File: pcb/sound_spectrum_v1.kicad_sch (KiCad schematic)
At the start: 33 parts, among them IC1-L1 ICS-43432, IC2-R1 ICS-43432, J1 SWD_CONN, J2 Conn_02x10_Counter_Clockwise, P1 USB_C_Plug_USB2.0, SW2 SW_DPST_x2, U1 STM32G473CBTx, U2 AP2112K-3.3, U3 USBLC6-2SC6, Y2 SG-210STF 48.0000ML5

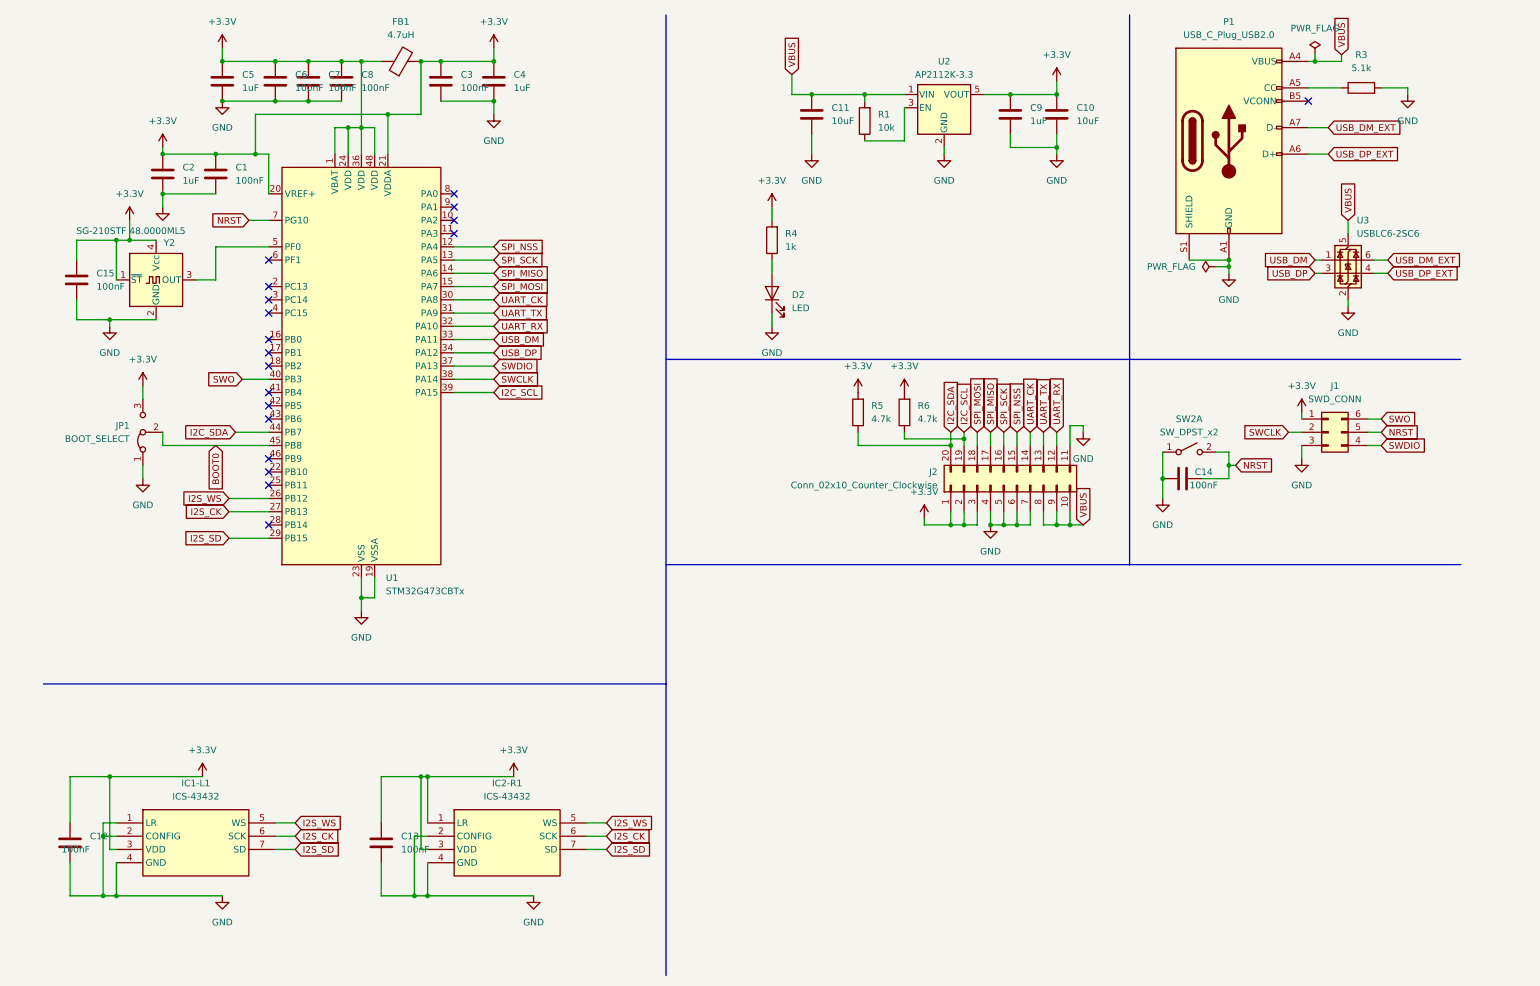
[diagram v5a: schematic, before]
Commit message: feat: add mounting holes
chore: change usb c receptor

chore: align microphones
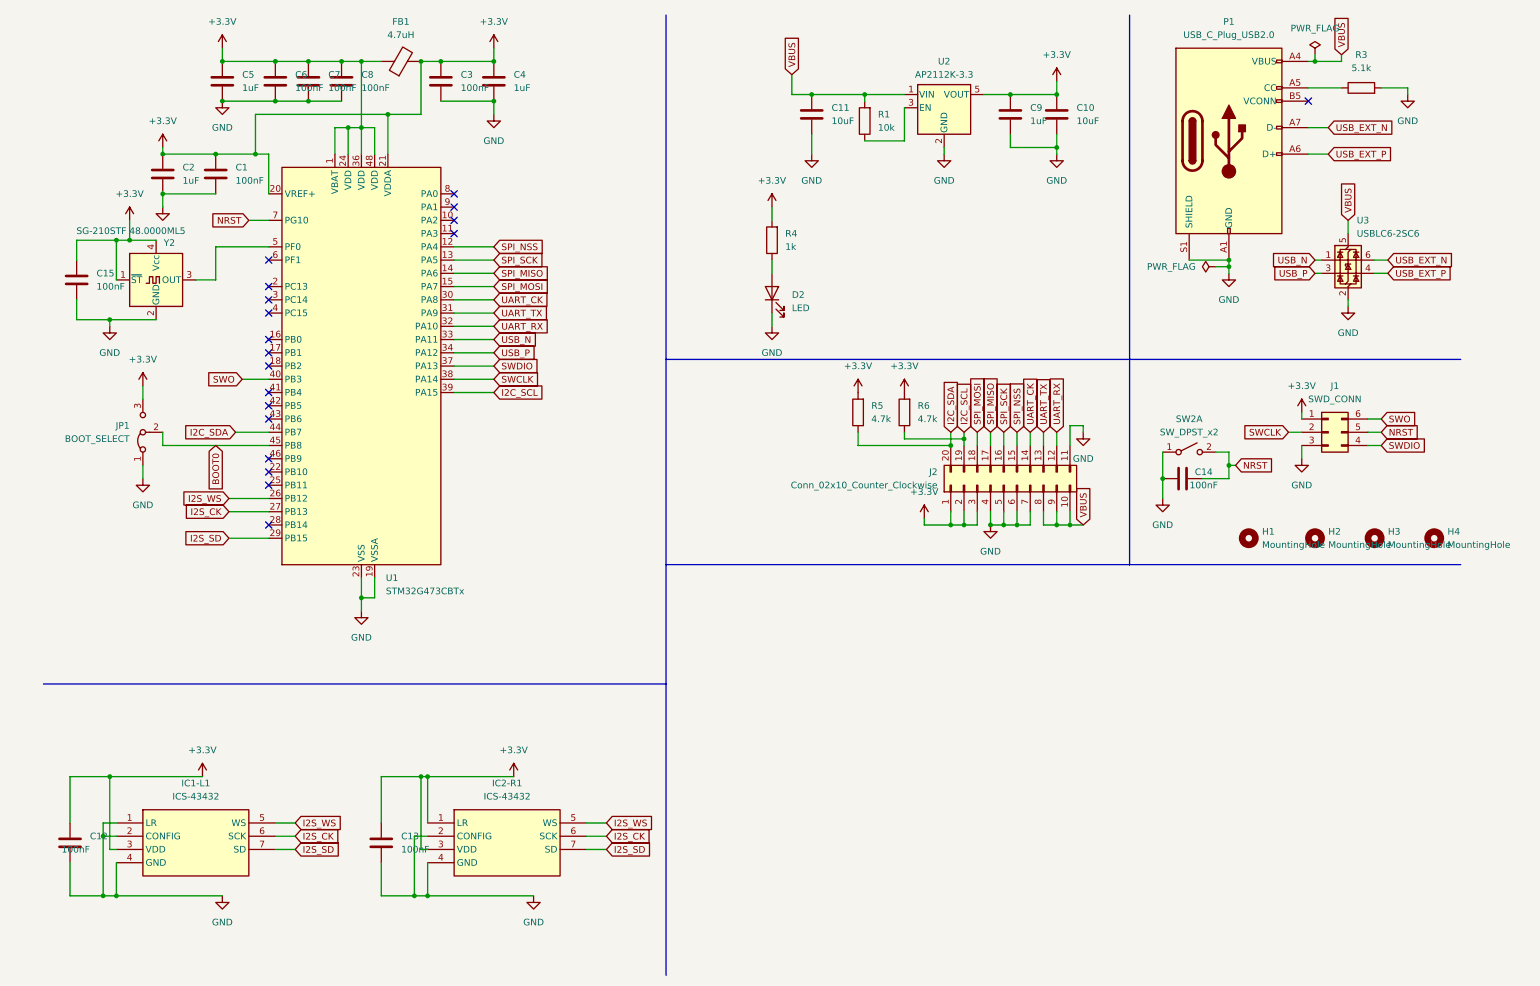
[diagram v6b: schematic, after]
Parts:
- added H1, H2, H3, H4: MountingHole, MountingHole:MountingHole_3.2mm_M3_DIN965, symbol Mechanical:MountingHole
- P1: footprint Connector_USB:USB_C_Receptacle_GCT_USB4085 -> Connector_USB:USB_C_Receptacle_GCT_USB4105-xx-A_16P_TopMnt_Horizontal
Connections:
- net USB_DM renamed USB_N
- net USB_DM_EXT renamed USB_EXT_N
- net USB_DP renamed USB_P
- net USB_DP_EXT renamed USB_EXT_P

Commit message: chore: add extra led
chore: minor changes
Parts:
- removed Y2: SG-210STF 48.0000ML5, Oscillator:Oscillator_SMD_SeikoEpson_SG210-4Pin_2.5x2.0mm, symbol Oscillator:SG-211
- added C16: 33pF, Capacitor_SMD:C_0805_2012Metric_Pad1.18x1.45mm_HandSolder, symbol Device:C
- added D1: LED - Green, LED_SMD:LED_0805_2012Metric_Pad1.15x1.40mm_HandSolder, symbol Device:LED
- added R2: 1k, Resistor_SMD:R_0805_2012Metric_Pad1.20x1.40mm_HandSolder, symbol Device:R
- added Y1: ABMM2-24.000MHZ-E2-T, ABMM2, symbol Samacsys:ABMM2-24.000MHZ-E2-T
- C15: value 100nF -> 33pF; Manufacturer_Part_Number 581-KGM21NR71E104KM -> 80-C0805C105Z4VAC
- D2: value LED -> LED - Red
- FB1: value 4.7uH -> ~
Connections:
- net +3.3V: no longer C15.1
- net GND: now also C16.2, D1.1 (K), Y1.2 (GND_1), Y1.4 (GND_2)
- net at U1.5 (PF0): now also C16.1, Y1.3 (X2)
- net LED_DBG: now reaches U1.25 (PB11)
- net LED_DBG: now also R2.2
- net at U1.6 (PF1): now also C15.1, Y1.1 (X1)
- new net: D1.2 (A), R2.1
- no-connect marks 19 -> 17

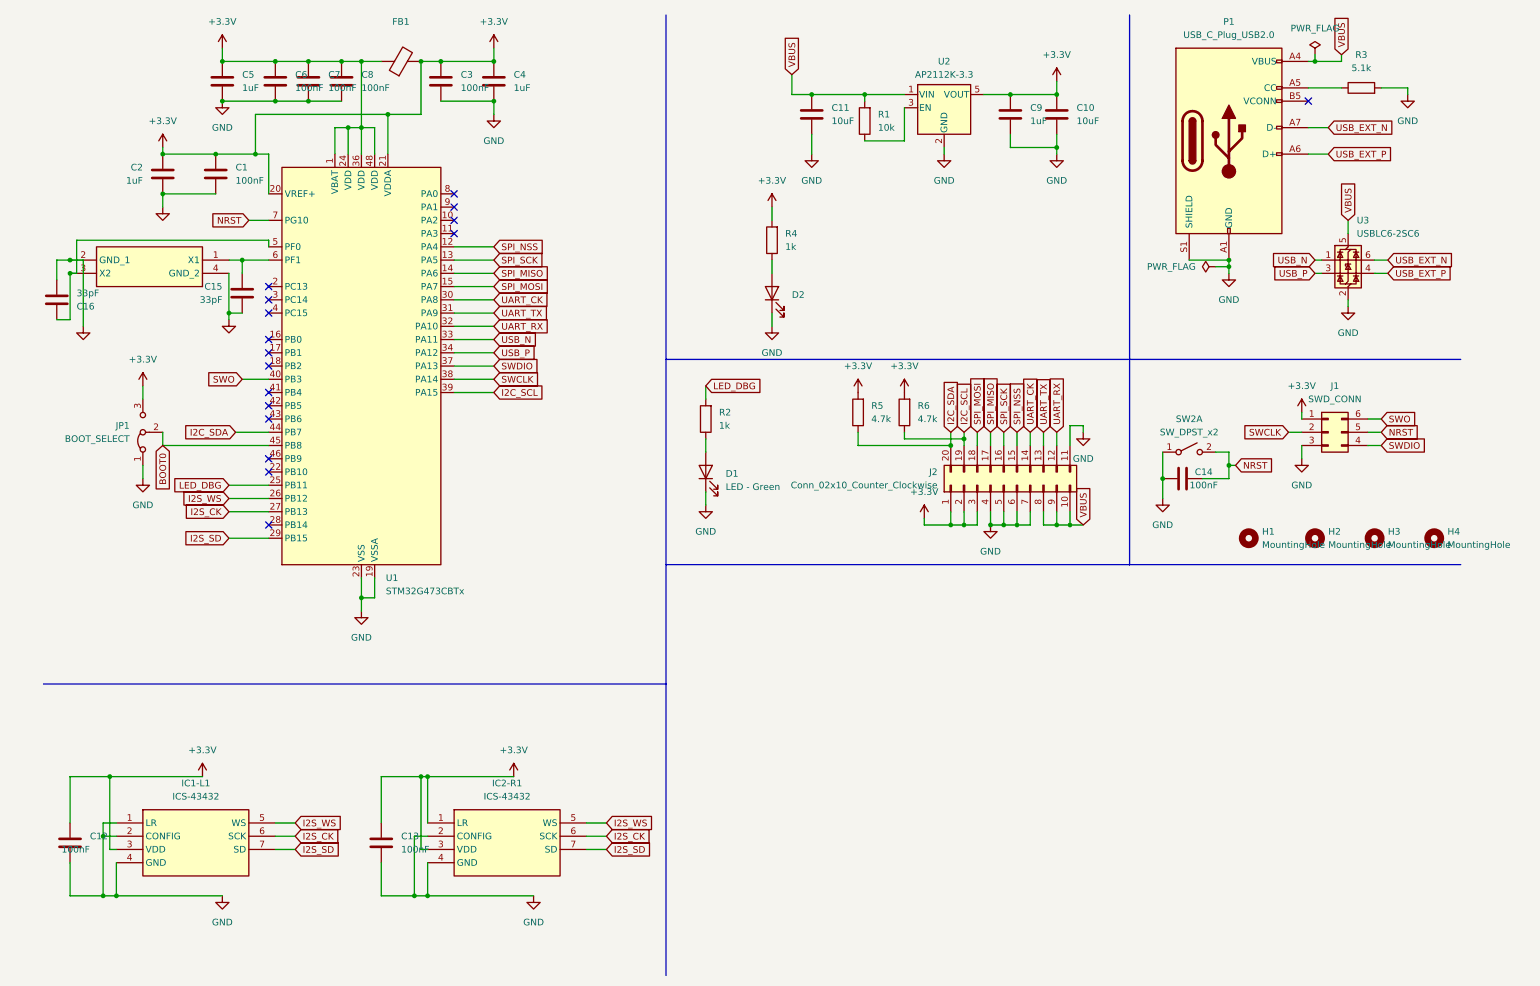
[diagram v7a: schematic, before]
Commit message: chore: add text in schematic
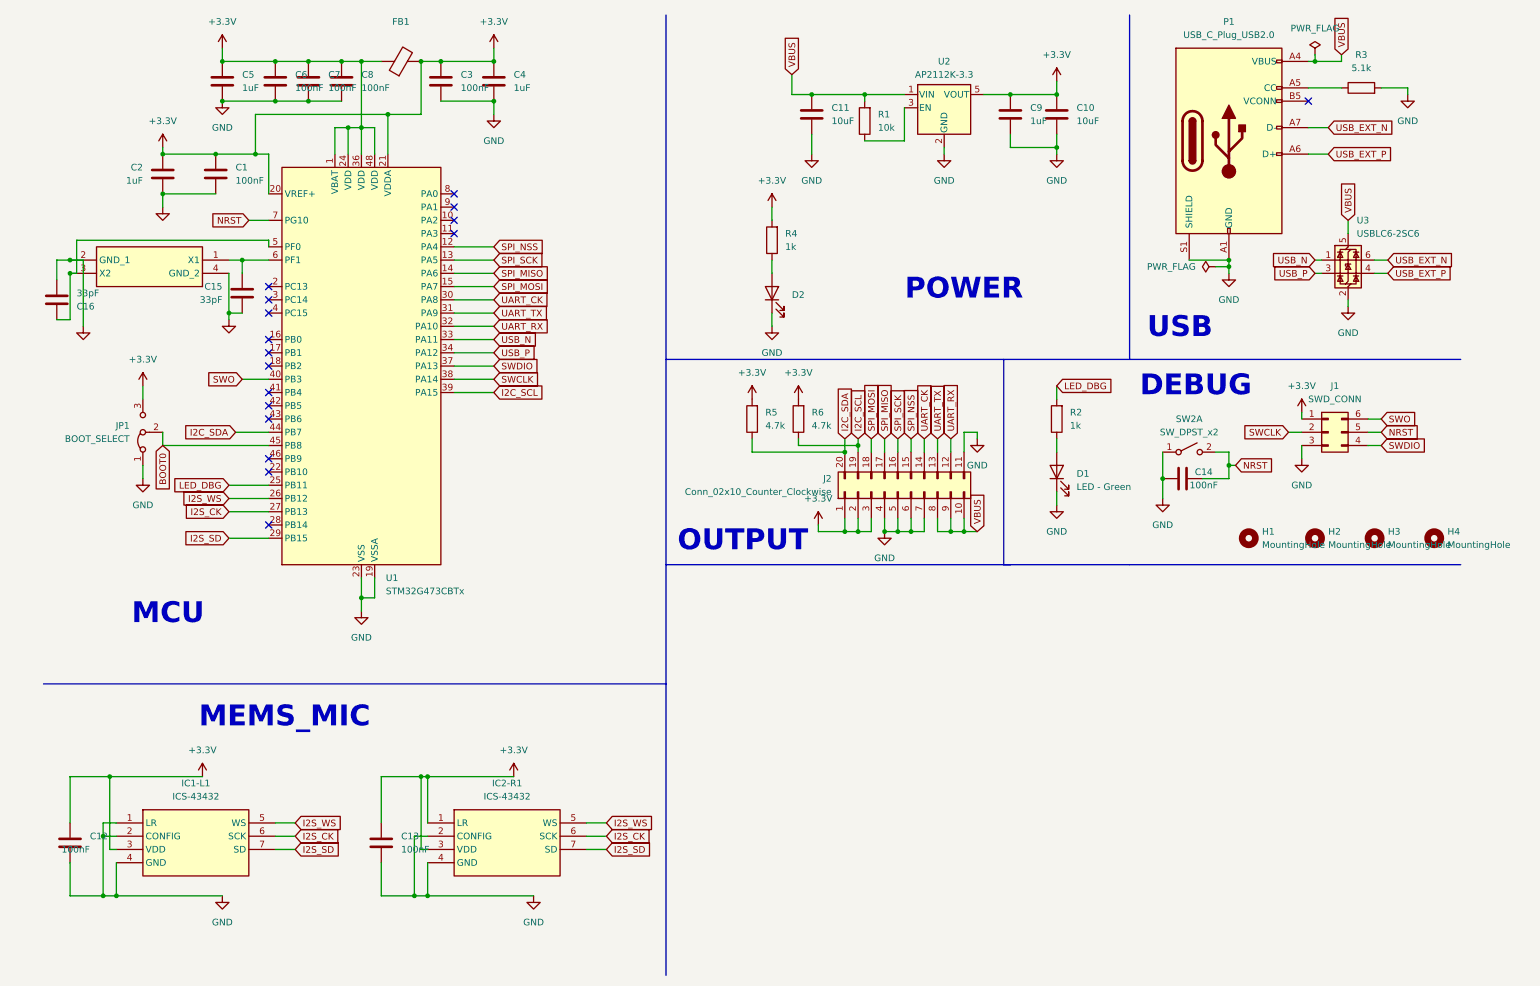
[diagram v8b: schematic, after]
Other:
- note added: "DEBUG"
- note added: "MCU"
- note added: "MEMS_MIC"
- note added: "OUTPUT"
- note added: "POWER"
- note added: "USB"
- moved on the sheet: D1, J2, R2, R5, R6
